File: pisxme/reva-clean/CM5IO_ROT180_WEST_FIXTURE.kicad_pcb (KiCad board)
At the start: 6 copper layers, 300 x 180 mm, 72 parts, among them J1 74221-101LF, J2 A70-112-331N126, J3 JAE SM3ZS067U410ABR1000 B-key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, J4 Amphenol 10171746-00021LF USB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, J5 0039300020, J6 0039300020, J7 Raspberry-Pi-5-Compute-Module, Q1 CSD19536KCS, Q2 CSD19536KCS, U1 LM74700QDBVRQ1, U2 LM74700QDBVRQ1, U3 TPSM63606RDLR, U4 TPSM63606RDLR, U5 TPSM63606RDLR, U6 TPD4EUSB30, U7 TUSB9261IPVP, U8 Texas_DRT_3, U9 TPD4EUSB30

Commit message: phase17: isolate rotated ethernet fixture evidence
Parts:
- removed C1, C18, C2, C24, C9: C_0805_2012Metric, C_0805_2012Metric
- removed C14, C15, C23, C25, C5, C6: , C_1206_3216Metric
- removed C16, C17, C19, C26, C27, C28, C29, C30, C31, C32, C33, C34, C35, C36, C37, C38, C39, C40, C41, C7, C8: , C_1210_3225Metric
- removed C3, C4: C_0603_1608Metric, C_0603_1608Metric
- removed D1, D2: SMBJ18A, TVS_SMBJ18A_DO214AA
- removed F1, F2: 178.6165.0001, ATO_FuseHolder_17861650001
- removed J1: 74221-101LF, PiSXMeRevAClean_SXM2_74221_101LF
- removed J3: JAE SM3ZS067U410ABR1000 B-key SATA socket, JAE_SM3ZS067U410ABR1000_BKEY
- removed J4: Amphenol 10171746-00021LF USB-C USB2 SERVICE, USB_C_SERVICE_10171746
- removed J5, J6: 0039300020, Molex_0039300020_5569_2P_RA
- removed MECH_M2_2280: JAE SM3ZS067U410ABR1000 / 2280 card envelope, M2_2280_RETENTION_ENVELOPE
- removed MECH_V100: REV_A_EMPIRICAL_RISK: 150x95mm cooler/backplate envelope, V100_COOLER_BACKPLATE_ENVELOPE
- removed Q1, Q2: CSD19536KCS, CSD19536KCS_TO220
- removed R1, R11, R12, R13, R14, R19, R2, R20, R21, R22, R3, R4, R5, R6: R_0402_1005Metric, R_0402_1005Metric
- removed U1, U2: LM74700QDBVRQ1, LM74700QDBVRQ1_SOT23_6
- removed U3, U4, U5: TPSM63606RDLR, TPSM63606RDLR_RDL0020
- removed U7: TUSB9261IPVP, TUSB9261IPVP_HTQFP64
- removed U8: Texas_DRT_3, Texas_DRT_3
- J7: moved to F.Cu
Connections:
- J2 pad 11: /ETHERNET/ETH_CT1 -> (no net)
- J2 pad 12: /ETHERNET/ETH_CT2 -> (no net)
- J2 pad 13: /ETHERNET/ETH_CT3 -> (no net)
- J2 pad 14: /ETHERNET/ETH_CT4 -> (no net)
- J2 pad 15: /ETHERNET/GBE_LED_Y_A -> (no net)
- J2 pad 16: /ETHERNET/GBE_LED_Y_K -> (no net)
- J2 pad 17: /ETHERNET/GBE_LED_G_A -> (no net)
- J2 pad 18: /ETHERNET/GBE_LED_G_K -> (no net)
- J2 pad 19: /ETHERNET/GBE_SHIELD -> (no net)
- J2 pad 20: /ETHERNET/GBE_SHIELD -> (no net)
- J7 pad 1: /CORE_CM5/POWER_GND -> (no net)
- J7 pad 100: unconnected-(J7A-CAM_GPIO1-Pad100) -> (no net)
- J7 pad 101: unconnected-(J7B-USB_OTG_ID-Pad101) -> (no net)
- J7 pad 102: unconnected-(J7B-PCIe_nCLKREQ-Pad102) -> (no net)
- J7 pad 103: unconnected-(J7B-USB2_N-Pad103) -> (no net)
- J7 pad 104: unconnected-(J7B-PCIE_nWAKE-Pad104) -> (no net)
- J7 pad 105: unconnected-(J7B-USB2_P-Pad105) -> (no net)
- J7 pad 106: unconnected-(J7B-PCIE_PWR_EN-Pad106) -> (no net)
- J7 pad 107: /CORE_CM5/POWER_GND -> (no net)
- J7 pad 108: /CORE_CM5/POWER_GND -> (no net)
- J7 pad 109: /CORE_CM5/CM5_PERST -> (no net)
- J7 pad 110: /CORE_CM5/CM5_REFCLK_P -> (no net)
- J7 pad 111: unconnected-(J7B-VBUS_EN-Pad111) -> (no net)
- J7 pad 112: /CORE_CM5/CM5_REFCLK_N -> (no net)
- J7 pad 113: /CORE_CM5/POWER_GND -> (no net)
- J7 pad 114: /CORE_CM5/POWER_GND -> (no net)
- J7 pad 115: unconnected-(J7B-MIPI0_D0_N-Pad115) -> (no net)
- J7 pad 116: /CORE_CM5/CM5_PER0_P -> (no net)
- J7 pad 117: unconnected-(J7B-MIPI0_D0_P-Pad117) -> (no net)
- J7 pad 118: /CORE_CM5/CM5_PER0_N -> (no net)
- J7 pad 119: /CORE_CM5/POWER_GND -> (no net)
- J7 pad 120: /CORE_CM5/POWER_GND -> (no net)
- J7 pad 121: unconnected-(J7B-MIPI0_D1_N-Pad121) -> (no net)
- J7 pad 122: /CORE_CM5/CM5_PET0_P -> (no net)
- J7 pad 123: unconnected-(J7B-MIPI0_D1_P-Pad123) -> (no net)
- J7 pad 124: /CORE_CM5/CM5_PET0_N -> (no net)
- J7 pad 125: /CORE_CM5/POWER_GND -> (no net)
- J7 pad 126: /CORE_CM5/POWER_GND -> (no net)
- J7 pad 127: unconnected-(J7B-MIPI0_C_N-Pad127) -> (no net)
- J7 pad 128: /CORE_CM5/CM5_USB3_RX_N -> (no net)
- J7 pad 129: unconnected-(J7B-MIPI0_C_P-Pad129) -> (no net)
- J7 pad 13: /CORE_CM5/POWER_GND -> (no net)
- J7 pad 130: /CORE_CM5/CM5_USB3_RX_P -> (no net)
- J7 pad 131: /CORE_CM5/POWER_GND -> (no net)
- J7 pad 132: /CORE_CM5/POWER_GND -> (no net)
- J7 pad 133: unconnected-(J7B-MIPI0_D2_N-Pad133) -> (no net)
- J7 pad 134: unconnected-(J7B-USB3-0-D_P-Pad134) -> (no net)
- J7 pad 135: unconnected-(J7B-MIPI0_D2_P-Pad135) -> (no net)
- J7 pad 136: unconnected-(J7B-USB3-0-D_N-Pad136) -> (no net)
- J7 pad 137: /CORE_CM5/POWER_GND -> (no net)
- J7 pad 138: /CORE_CM5/POWER_GND -> (no net)
- J7 pad 139: unconnected-(J7B-MIPI0_D3_N-Pad139) -> (no net)
- J7 pad 14: /CORE_CM5/POWER_GND -> (no net)
- J7 pad 140: /CORE_CM5/CM5_USB3_TX_N -> (no net)
- J7 pad 141: unconnected-(J7B-MIPI0_D3_P-Pad141) -> (no net)
- J7 pad 142: /CORE_CM5/CM5_USB3_TX_P -> (no net)
- J7 pad 143: unconnected-(J7B-HDMI1_HOTPLUG-Pad143) -> (no net)
- J7 pad 144: /CORE_CM5/POWER_GND -> (no net)
- J7 pad 145: unconnected-(J7B-HDMI1_SDA-Pad145) -> (no net)
- J7 pad 146: unconnected-(J7B-HDMI1_TX2_P-Pad146) -> (no net)
- J7 pad 147: unconnected-(J7B-HDMI1_SCL-Pad147) -> (no net)
- J7 pad 148: unconnected-(J7B-HDMI1_TX2_N-Pad148) -> (no net)
- J7 pad 149: unconnected-(J7B-HDMI1_CEC-Pad149) -> (no net)
- J7 pad 15: unconnected-(J7A-Ethernet_nLED3(3.3v)-Pad15) -> (no net)
- J7 pad 150: /CORE_CM5/POWER_GND -> (no net)
- J7 pad 151: unconnected-(J7B-HDMI0_CEC-Pad151) -> (no net)
- J7 pad 152: unconnected-(J7B-HDMI1_TX1_P-Pad152) -> (no net)
- J7 pad 153: unconnected-(J7B-HDMI0_HOTPLUG-Pad153) -> (no net)
- J7 pad 154: unconnected-(J7B-HDMI1_TX1_N-Pad154) -> (no net)
- J7 pad 155: /CORE_CM5/POWER_GND -> (no net)
- J7 pad 156: /CORE_CM5/POWER_GND -> (no net)
- J7 pad 157: unconnected-(J7B-USB3-1-RX_N-Pad157) -> (no net)
- J7 pad 158: unconnected-(J7B-HDMI1_TX0_P-Pad158) -> (no net)
- J7 pad 159: unconnected-(J7B-USB3-1-RX_P-Pad159) -> (no net)
- J7 pad 16: unconnected-(J7A-FAN_TACHO-Pad16) -> (no net)
- J7 pad 160: unconnected-(J7B-HDMI1_TX0_N-Pad160) -> (no net)
- J7 pad 161: /CORE_CM5/POWER_GND -> (no net)
- J7 pad 162: /CORE_CM5/POWER_GND -> (no net)
- J7 pad 163: unconnected-(J7B-USB3-1-D_P-Pad163) -> (no net)
- J7 pad 164: unconnected-(J7B-HDMI1_CLK_P-Pad164) -> (no net)
- J7 pad 165: unconnected-(J7B-USB3-1-D_N-Pad165) -> (no net)
- J7 pad 166: unconnected-(J7B-HDMI1_CLK_N-Pad166) -> (no net)
- J7 pad 167: /CORE_CM5/POWER_GND -> (no net)
- J7 pad 168: /CORE_CM5/POWER_GND -> (no net)
- J7 pad 169: unconnected-(J7B-USB3-1-TX_N-Pad169) -> (no net)
- J7 pad 17: unconnected-(J7A-Ethernet_nLED2(3.3v)-Pad17) -> (no net)
- J7 pad 170: unconnected-(J7B-HDMI0_TX2_P-Pad170) -> (no net)
- J7 pad 171: unconnected-(J7B-USB3-1-TX_P-Pad171) -> (no net)
- J7 pad 172: unconnected-(J7B-HDMI0_TX2_N-Pad172) -> (no net)
- J7 pad 173: /CORE_CM5/POWER_GND -> (no net)
- J7 pad 174: /CORE_CM5/POWER_GND -> (no net)
- J7 pad 175: unconnected-(J7B-MIPI1_D0_N-Pad175) -> (no net)
- J7 pad 176: unconnected-(J7B-HDMI0_TX1_P-Pad176) -> (no net)
- J7 pad 177: unconnected-(J7B-MIPI1_D0_P-Pad177) -> (no net)
- J7 pad 178: unconnected-(J7B-HDMI0_TX1_N-Pad178) -> (no net)
- J7 pad 179: /CORE_CM5/POWER_GND -> (no net)
- J7 pad 18: unconnected-(J7A-Ethernet_SYNC_OUT(3.3v)-Pad18) -> (no net)
- J7 pad 180: /CORE_CM5/POWER_GND -> (no net)
- J7 pad 181: unconnected-(J7B-MIPI1_D1_N-Pad181) -> (no net)
- J7 pad 182: unconnected-(J7B-HDMI0_TX0_P-Pad182) -> (no net)
- J7 pad 183: unconnected-(J7B-MIPI1_D1_P-Pad183) -> (no net)
- J7 pad 184: unconnected-(J7B-HDMI0_TX0_N-Pad184) -> (no net)
- J7 pad 185: /CORE_CM5/POWER_GND -> (no net)
- J7 pad 186: /CORE_CM5/POWER_GND -> (no net)
- J7 pad 187: unconnected-(J7B-MIPI1_C_N-Pad187) -> (no net)
- J7 pad 188: unconnected-(J7B-HDMI0_CLK_P-Pad188) -> (no net)
- J7 pad 189: unconnected-(J7B-MIPI1_C_P-Pad189) -> (no net)
- J7 pad 19: unconnected-(J7A-FAN_PWM-Pad19) -> (no net)
- J7 pad 190: unconnected-(J7B-HDMI0_CLK_N-Pad190) -> (no net)
- J7 pad 191: /CORE_CM5/POWER_GND -> (no net)
- J7 pad 192: /CORE_CM5/POWER_GND -> (no net)
- J7 pad 193: unconnected-(J7B-MIPI1_D2_N-Pad193) -> (no net)
- J7 pad 194: unconnected-(J7B-MIPI1_D3_N-Pad194) -> (no net)
- J7 pad 195: unconnected-(J7B-MIPI1_D2_P-Pad195) -> (no net)
- J7 pad 196: unconnected-(J7B-MIPI1_D3_P-Pad196) -> (no net)
- J7 pad 197: /CORE_CM5/POWER_GND -> (no net)
- J7 pad 198: /CORE_CM5/POWER_GND -> (no net)
- J7 pad 199: unconnected-(J7B-HDMI0_SDA-Pad199) -> (no net)
- J7 pad 2: /CORE_CM5/POWER_GND -> (no net)
- J7 pad 20: unconnected-(J7A-EEPROM_nWP-Pad20) -> (no net)
- J7 pad 200: unconnected-(J7B-HDMI0_SCL-Pad200) -> (no net)
- J7 pad 21: unconnected-(J7A-LED_nACT-Pad21) -> (no net)
- J7 pad 22: /CORE_CM5/POWER_GND -> (no net)
- J7 pad 23: /CORE_CM5/POWER_GND -> (no net)
- J7 pad 24: unconnected-(J7A-GPIO26-Pad24) -> (no net)
- J7 pad 25: unconnected-(J7A-GPIO21-Pad25) -> (no net)
- J7 pad 26: unconnected-(J7A-GPIO19-Pad26) -> (no net)
- J7 pad 27: unconnected-(J7A-GPIO20-Pad27) -> (no net)
- J7 pad 28: unconnected-(J7A-GPIO13-Pad28) -> (no net)
- J7 pad 29: unconnected-(J7A-GPIO16-Pad29) -> (no net)
- J7 pad 30: unconnected-(J7A-GPIO6-Pad30) -> (no net)
- J7 pad 31: unconnected-(J7A-GPIO12-Pad31) -> (no net)
- J7 pad 32: /CORE_CM5/POWER_GND -> (no net)
- J7 pad 33: /CORE_CM5/POWER_GND -> (no net)
- J7 pad 34: unconnected-(J7A-GPIO5-Pad34) -> (no net)
- J7 pad 35: unconnected-(J7A-ID_SC-Pad35) -> (no net)
- J7 pad 36: unconnected-(J7A-ID_SD-Pad36) -> (no net)
- J7 pad 37: unconnected-(J7A-GPIO7-Pad37) -> (no net)
- J7 pad 38: unconnected-(J7A-GPIO11-Pad38) -> (no net)
- J7 pad 39: unconnected-(J7A-GPIO8-Pad39) -> (no net)
- J7 pad 40: unconnected-(J7A-GPIO9-Pad40) -> (no net)
- J7 pad 41: unconnected-(J7A-GPIO25-Pad41) -> (no net)
- J7 pad 42: /CORE_CM5/POWER_GND -> (no net)
- J7 pad 43: /CORE_CM5/POWER_GND -> (no net)
- J7 pad 44: unconnected-(J7A-GPIO10-Pad44) -> (no net)
- J7 pad 45: unconnected-(J7A-GPIO24-Pad45) -> (no net)
- J7 pad 46: unconnected-(J7A-GPIO22-Pad46) -> (no net)
- J7 pad 47: unconnected-(J7A-GPIO23-Pad47) -> (no net)
- J7 pad 48: unconnected-(J7A-GPIO27-Pad48) -> (no net)
- J7 pad 49: unconnected-(J7A-GPIO18-Pad49) -> (no net)
- J7 pad 50: unconnected-(J7A-GPIO17-Pad50) -> (no net)
- J7 pad 51: unconnected-(J7A-GPIO15-Pad51) -> (no net)
- J7 pad 52: /CORE_CM5/POWER_GND -> (no net)
- J7 pad 53: /CORE_CM5/POWER_GND -> (no net)
- J7 pad 54: unconnected-(J7A-GPIO4-Pad54) -> (no net)
- J7 pad 55: unconnected-(J7A-GPIO14-Pad55) -> (no net)
- J7 pad 56: unconnected-(J7A-GPIO3-Pad56) -> (no net)
- J7 pad 57: unconnected-(J7A-SD_CLK-Pad57) -> (no net)
- J7 pad 58: unconnected-(J7A-GPIO2-Pad58) -> (no net)
- J7 pad 59: /CORE_CM5/POWER_GND -> (no net)
- J7 pad 60: /CORE_CM5/POWER_GND -> (no net)
- J7 pad 61: unconnected-(J7A-SD_DAT3-Pad61) -> (no net)
- J7 pad 62: unconnected-(J7A-SD_CMD-Pad62) -> (no net)
- J7 pad 63: unconnected-(J7A-SD_DAT0-Pad63) -> (no net)
- J7 pad 64: unconnected-(J7A-SD_DAT5-Pad64) -> (no net)
- J7 pad 65: /CORE_CM5/POWER_GND -> (no net)
- J7 pad 66: /CORE_CM5/POWER_GND -> (no net)
- J7 pad 67: unconnected-(J7A-SD_DAT1-Pad67) -> (no net)
- J7 pad 68: unconnected-(J7A-SD_DAT4-Pad68) -> (no net)
- J7 pad 69: unconnected-(J7A-SD_DAT2-Pad69) -> (no net)
- J7 pad 7: /CORE_CM5/POWER_GND -> (no net)
- J7 pad 70: unconnected-(J7A-SD_DAT7-Pad70) -> (no net)
- J7 pad 71: /CORE_CM5/POWER_GND -> (no net)
- J7 pad 72: unconnected-(J7A-SD_DAT6-Pad72) -> (no net)
- J7 pad 73: unconnected-(J7A-SD_VDD_Override-Pad73) -> (no net)
- J7 pad 74: /CORE_CM5/POWER_GND -> (no net)
- J7 pad 75: unconnected-(J7A-SD_PWR_ON-Pad75) -> (no net)
- J7 pad 76: unconnected-(J7A-VBAT-Pad76) -> (no net)
- J7 pad 77: /CORE_CM5/CM5_5V -> (no net)
- J7 pad 78: unconnected-(J7A-GPIO_VREF(1.8v/3.3v_Input)-Pad78) -> (no net)
- J7 pad 79: /CORE_CM5/CM5_5V -> (no net)
- J7 pad 8: /CORE_CM5/POWER_GND -> (no net)
- J7 pad 80: unconnected-(J7A-SCL0-Pad80) -> (no net)
- J7 pad 81: /CORE_CM5/CM5_5V -> (no net)
- J7 pad 82: unconnected-(J7A-SDA0-Pad82) -> (no net)
- J7 pad 83: /CORE_CM5/CM5_5V -> (no net)
- J7 pad 84: unconnected-(J7A-+3.3v_(Output)-Pad84) -> (no net)
- J7 pad 85: /CORE_CM5/CM5_5V -> (no net)
- J7 pad 86: unconnected-(J7A-+3.3v_(Output)-Pad86) -> (no net)
- J7 pad 87: /CORE_CM5/CM5_5V -> (no net)
- J7 pad 88: unconnected-(J7A-+1.8v_(Output)-Pad88) -> (no net)
- J7 pad 89: unconnected-(J7A-WiFi_nDisable-Pad89) -> (no net)
- J7 pad 90: unconnected-(J7A-+1.8v_(Output)-Pad90) -> (no net)
- J7 pad 91: unconnected-(J7A-BT_nDisable-Pad91) -> (no net)
- J7 pad 92: unconnected-(J7A-PWR_BUT-Pad92) -> (no net)
- J7 pad 93: unconnected-(J7A-nRPIBOOT-Pad93) -> (no net)
- J7 pad 94: unconnected-(J7A-CC1-Pad94) -> (no net)
- J7 pad 95: unconnected-(J7A-LED_nPWR-Pad95) -> (no net)
- J7 pad 96: unconnected-(J7A-CC2-Pad96) -> (no net)
- J7 pad 97: unconnected-(J7A-CAM_GPIO0-Pad97) -> (no net)
- J7 pad 98: /CORE_CM5/POWER_GND -> (no net)
- J7 pad 99: unconnected-(J7A-PMIC_ENABLE-Pad99) -> (no net)
- U6 pad 3: /ETHERNET/ETH_GND -> (no net)
- U6 pad 8: /ETHERNET/ETH_GND -> (no net)
- U9 pad 3: /ETHERNET/ETH_GND -> (no net)
- U9 pad 8: /ETHERNET/ETH_GND -> (no net)
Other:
- board outline removed
- board text removed: "ETHERNET"
- board text removed: "M.2 2280 SERVICE"
- board text removed: "PHASE 11 ACREAGE FLOORPLAN — NO ROUTING"
- board text removed: "POWER INPUT"
- board text removed: "PiSXMe Rev A orientation study — NO ROUTING"
- board text removed: "REGULATORS"
- board text removed: "SERVICE / DEBUG"
- board text removed: "STORAGE BRIDGE"
- board text removed: "V100 COOLER + BACKPLATE KEEPout"

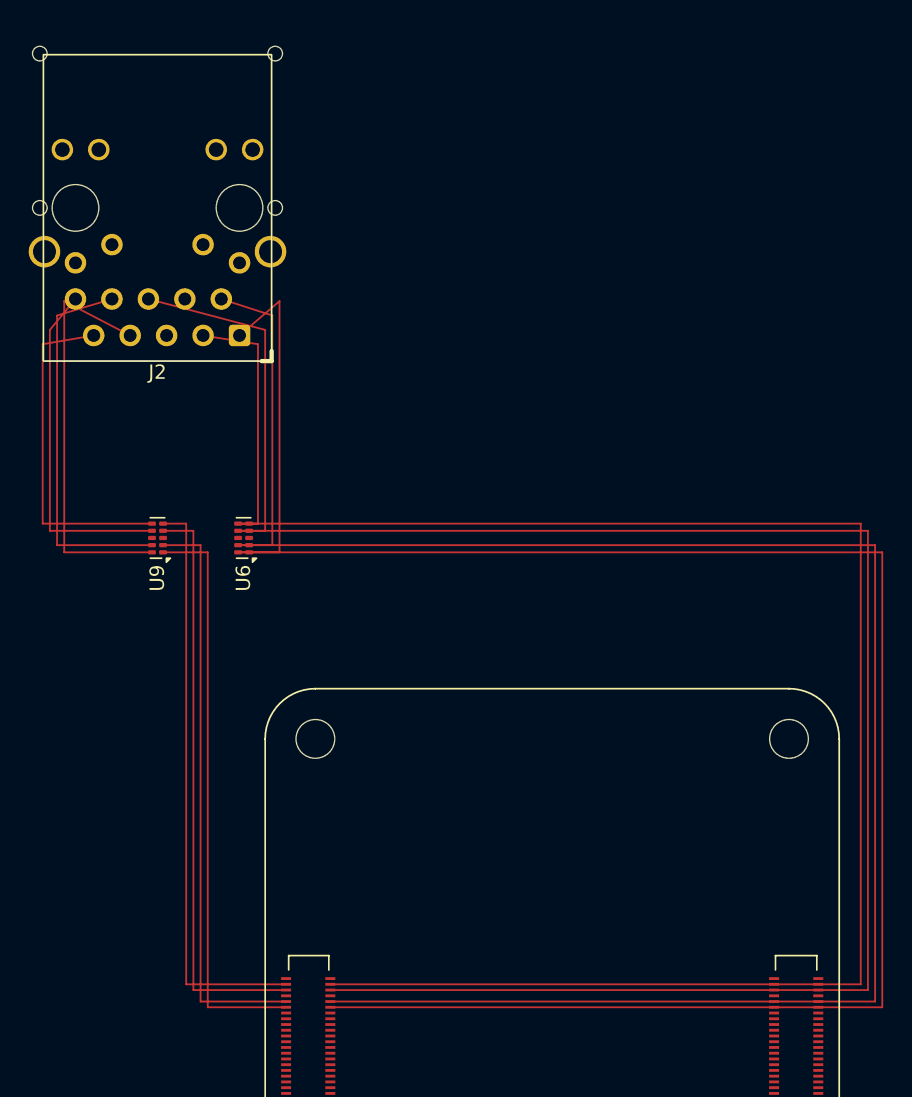
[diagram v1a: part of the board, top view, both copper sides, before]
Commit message: phase17: refine separated ethernet launch
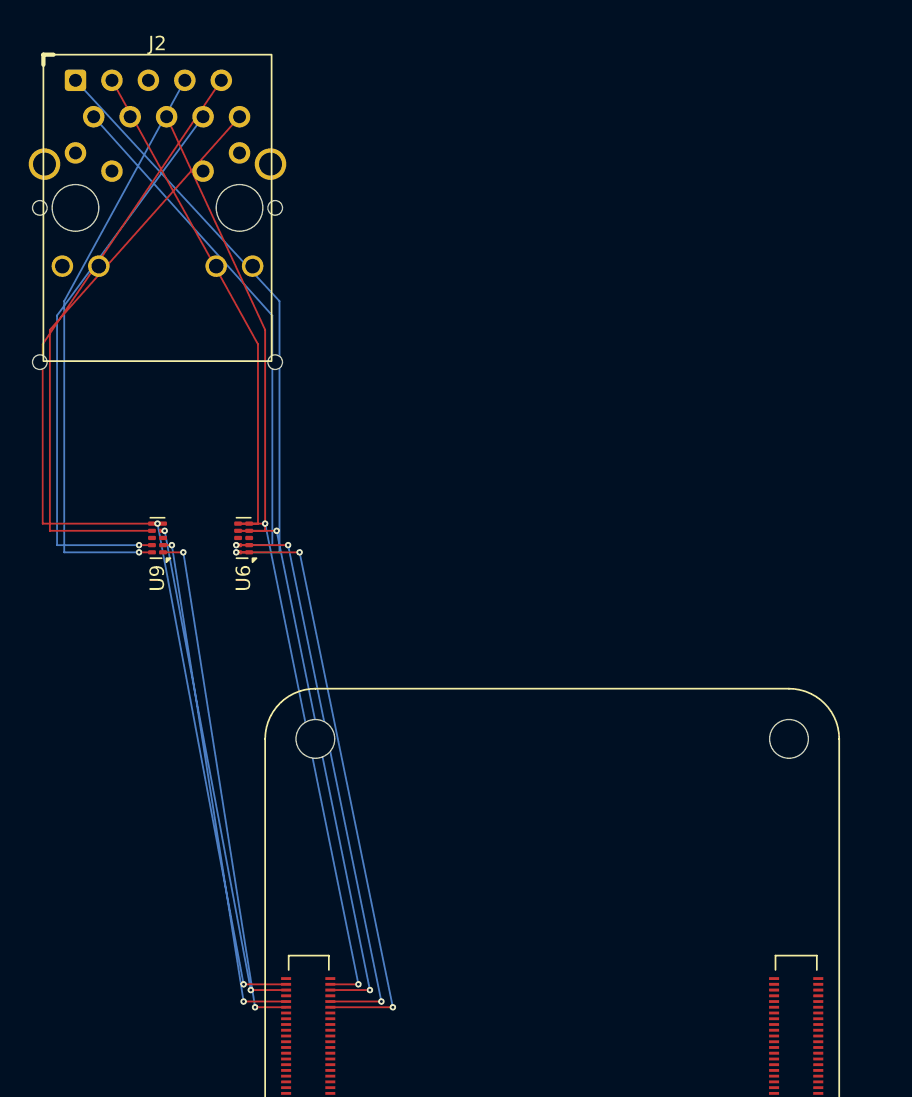
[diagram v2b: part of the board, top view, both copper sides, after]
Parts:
- turned J2 to 0 degrees
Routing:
- net CM5_GBE_TD1_N: track 137.6 -> 70.3 mm, vias 0 -> 2
- net CM5_GBE_TD0_N: track 136.3 -> 77.5 mm, vias 0 -> 3
- net CM5_GBE_TD1_P: track 130.2 -> 71.5 mm, vias 0 -> 2
- net CM5_GBE_TD0_P: track 139.1 -> 83.4 mm, vias 0 -> 3
- net CM5_GBE_TD3_P: track 64.4 -> 78.3 mm, vias 0 -> 2
- net CM5_GBE_TD3_N: track 64.5 -> 76.1 mm, vias 0 -> 2
- net CM5_GBE_TD2_N: track 67.0 -> 75.6 mm, vias 0 -> 3
- net CM5_GBE_TD2_P: track 69.1 -> 76.8 mm, vias 0 -> 3
